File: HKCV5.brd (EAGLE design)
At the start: 50 x 50 mm, 87 parts, among them Q1 CSD18540Q5BT, Q2 CSD18540Q5BT, Q3 CSD18540Q5BT, Q4 CSD18540Q5BT, Q5 CSD18540Q5BT, Q6 CSD18540Q5BT, U1 STM32F446VET6TR, U2 MCP2542FD-H/SN, U3 DRV8323SRTAT, U4 LMR16006XDDCR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

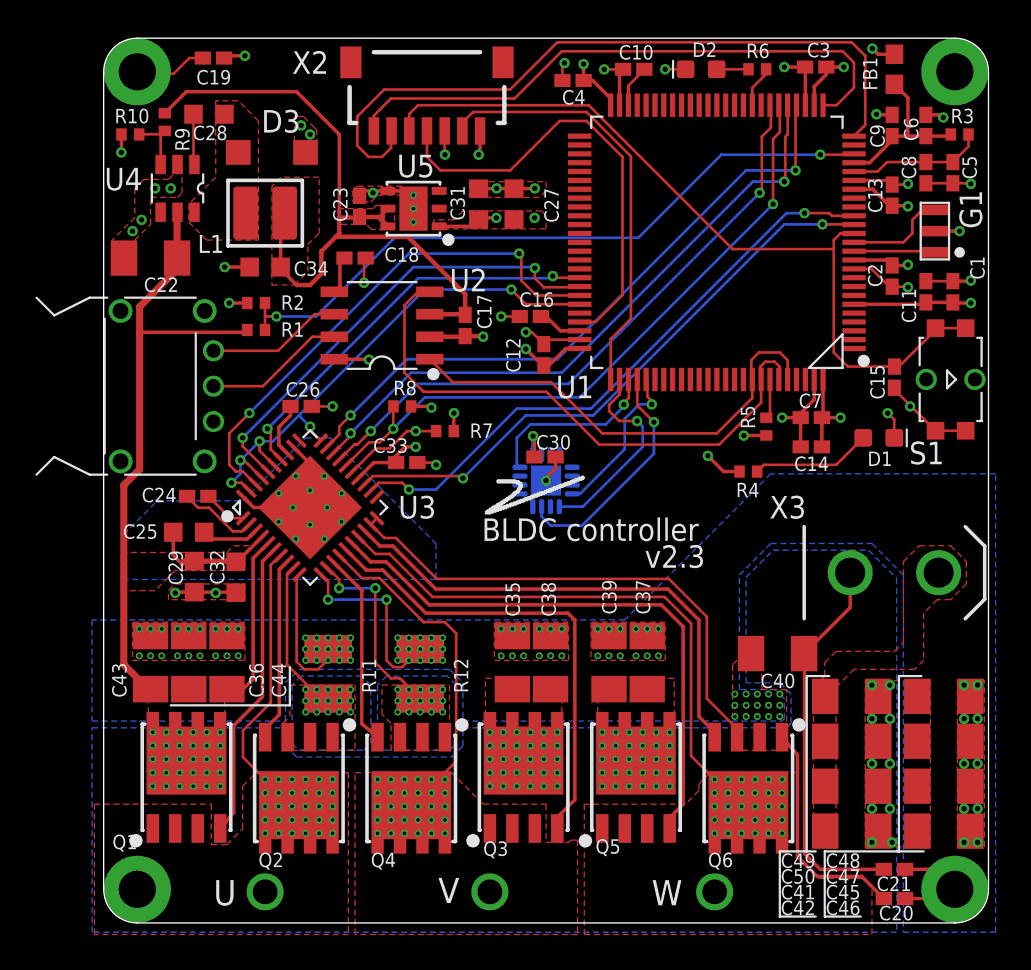
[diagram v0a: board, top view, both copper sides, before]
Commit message: CAP rated voltage increase, BOM
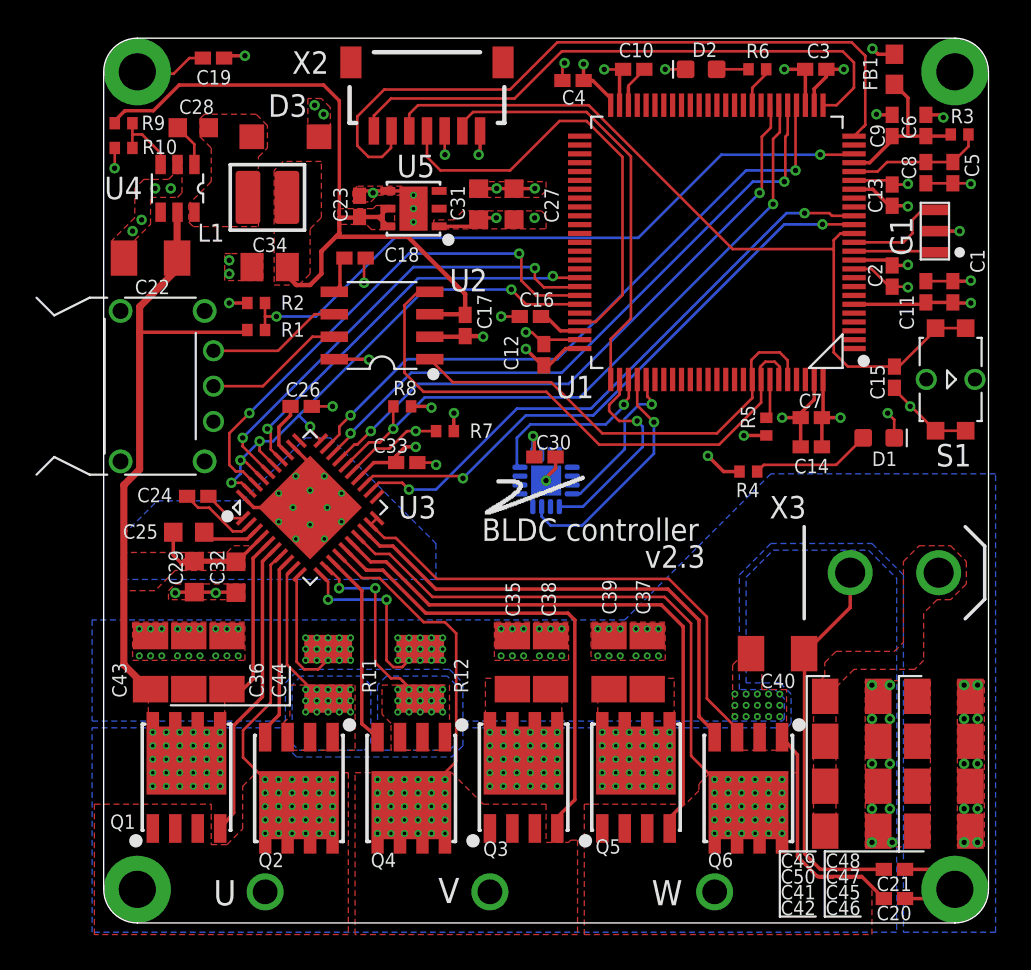
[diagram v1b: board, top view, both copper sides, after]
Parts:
- C17: value .1 uF 10v -> .1 uF 25v
- C23: value 1 uF 10v -> 1 uF 25v
- C34: value 22 uF 10v -> 22 uF 25V; device rcl:C0603K -> rcl:C0805K
- R11, R12: value .001 -> 1m
- moved R9 2.33 mm to (-23.9, 20.2), turned to 180 degrees
- moved C28 1.17 mm to (-19.9, 19.9)
- moved D3 1.17 mm to (-14.7, 19.4)
- moved L1 0.90 mm to (-15.7, 16.0)
- moved R10 0.85 mm to (-23.9, 18.8)
- moved C34 0.25 mm to (-15.6, 12.1)
- moved C3 0.13 mm to (15.2, 23.2)
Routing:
- net GND: track 140.6 -> 139.2 mm, vias 141 -> 142
- net +5V: track 43.3 -> 44.6 mm
- net FB: track 3.53 -> 4.08 mm

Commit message: Pre-final - board sent to JLCPCB on review
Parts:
- moved D1 9.14 mm to (9.78, 0.89), turned to 180 degrees
- moved C15 9.02 mm to (19.6, 14.9), turned to 90 degrees
- moved R4 7.85 mm to (19.1, 2.41), turned to 0 degrees
- moved C22 7.42 mm to (-15.0, 13.5), turned to 0 degrees
- moved C34 7.25 mm to (-14.2, 19.2), turned to 270 degrees
- moved R10 5.85 mm to (-23.5, 13.0), turned to 90 degrees
- moved R9 4.97 mm to (-23.5, 15.2), turned to 90 degrees
- moved L1 4.33 mm to (-18.0, 19.7), turned to 180 degrees
- moved D3 3.18 mm to (-14.6, 16.3)
- moved C28 2.54 mm to (-22.0, 18.4)
- moved U4 1.59 mm to (-20.1, 15.1), turned to 0 degrees
- moved C13 1.53 mm to (20.6, 17.3)
- moved C8 0.90 mm to (22.4, 17.5)
- moved C5 0.65 mm to (23.6, 17.5)
- moved R3 0.52 mm to (23.9, 19.7)
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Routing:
- net +24V: track 74.3 -> 78.6 mm
- net D1: track 6.78 -> 8.53 mm
- net VREF+: track 7.73 -> 9.01 mm
- net +5V: track 44.6 -> 45.8 mm
- net NRST: track 44.9 -> 44.1 mm, vias 0 -> 2
- net FB: track 4.08 -> 3.39 mm
- net GND: track 139.2 -> 138.6 mm, vias 142 -> 138
- net VDDA: track 9.50 -> 10.1 mm
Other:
- board text added: "Indicator"
- board text added: "Power"

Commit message: Mistakes discovered after using PCB
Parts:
- C29: device rcl:C0603K -> rcl:C1206K
- moved C29 1.35 mm to (-21.1, -4.83), turned to 180 degrees
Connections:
- removed net VIO: C18.1, U2.5
- net +3V3: now also C18.1, U2.5
- net GND: now also S1.2; no longer S1.3
- net NRST: now also S1.3; no longer S1.2
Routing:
- net +24V: track 78.6 -> 73.3 mm
- net NRST: track 44.1 -> 48.8 mm
- net +3V3: track 45.0 -> 48.5 mm, vias 16 -> 17
- net GND: track 138.6 -> 135.5 mm, vias 138 -> 141
- net VIO: track 2.14 -> 0.00 mm
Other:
- board text added: "v2.4"
- board text removed: "v2.3"
